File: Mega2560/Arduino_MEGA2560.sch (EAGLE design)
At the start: 8 parts

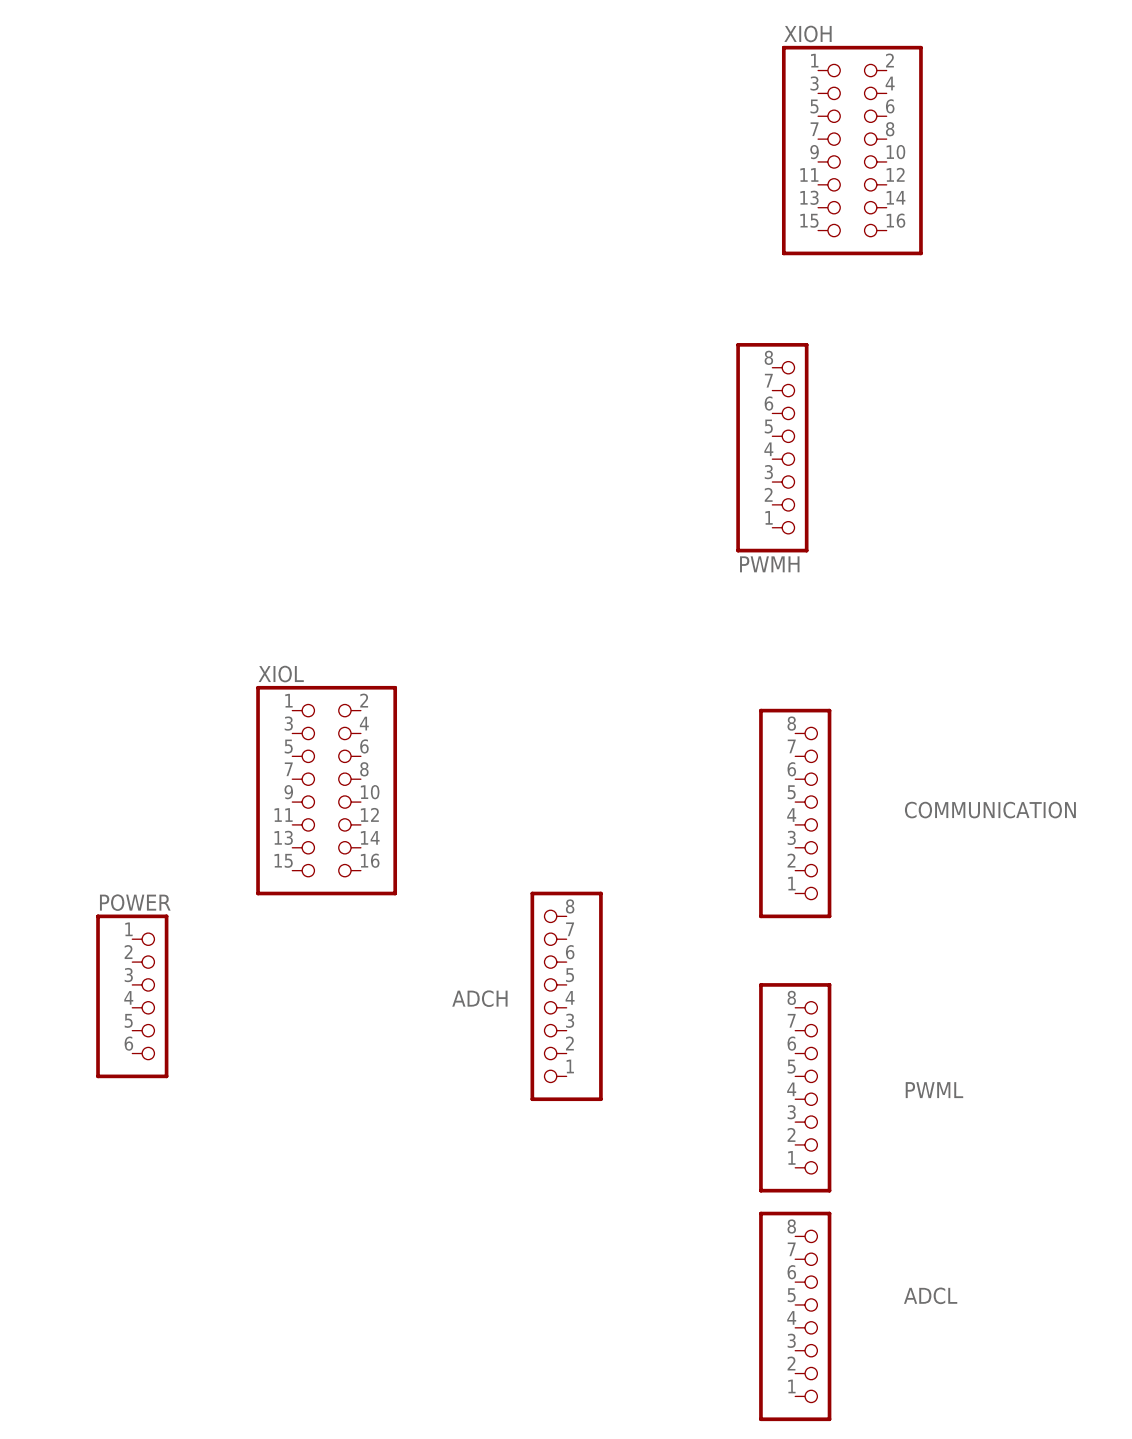
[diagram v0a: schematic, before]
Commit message: Arduino added ground pours
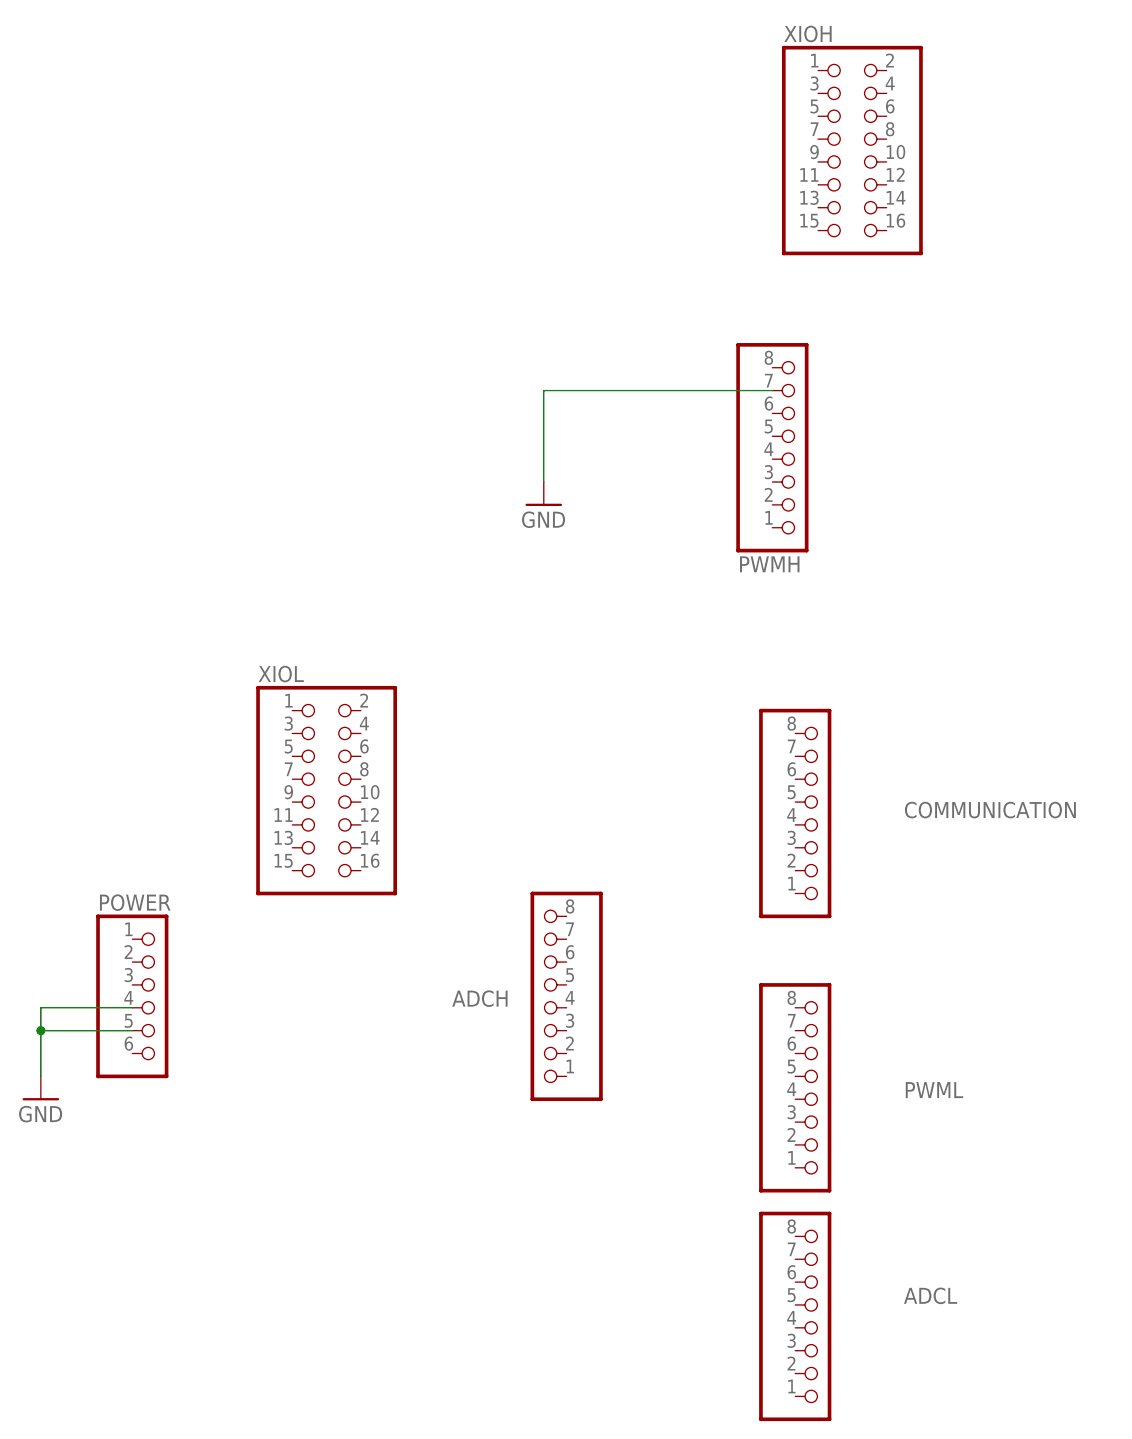
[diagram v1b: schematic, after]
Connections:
- new net GND: POWER.4, POWER.5, PWMH.7
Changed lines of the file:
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@@
 <part name="XIOH" library="pinhead" deviceset="PINHD-2X8" device=""/>
 <part name="XIOL" library="pinhead" deviceset="PINHD-2X8" device=""/>
+<part name="GND1" library="supply1" deviceset="GND" device=""/>
+<part name="GND2" library="supply1" deviceset="GND" device=""/>
 </parts>
 <sheets>
@@
 <instance part="XIOH" gate="A" x="101.6" y="137.16"/>
 <instance part="XIOL" gate="A" x="43.18" y="66.04"/>
+<instance part="GND1" gate="1" x="12.7" y="30.48"/>
+<instance part="GND2" gate="1" x="68.58" y="96.52"/>
 </instances>
 <busses>
 </busses>
 <nets>
+<net name="GND" class="0">
+<segment>
+<pinref part="POWER" gate="A" pin="4"/>
+<pinref part="GND1" gate="1" pin="GND"/>
+<wire x1="22.86" y1="40.64" x2="12.7" y2="40.64" width="0.1524" layer="91"/>
+<wire x1="12.7" y1="40.64" x2="12.7" y2="38.1" width="0.1524" layer="91"/>
+<pinref part="POWER" gate="A" pin="5"/>
+<wire x1="12.7" y1="38.1" x2="12.7" y2="33.02" width="0.1524" layer="91"/>
+<wire x1="22.86" y1="38.1" x2="12.7" y2="38.1" width="0.1524" layer="91"/>
+<junction x="12.7" y="38.1"/>
+</segment>
+<segment>
+<pinref part="PWMH" gate="A" pin="7"/>
+<pinref part="GND2" gate="1" pin="GND"/>
+<wire x1="93.98" y1="109.22" x2="68.58" y2="109.22" width="0.1524" layer="91"/>
+<wire x1="68.58" y1="109.22" x2="68.58" y2="99.06" width="0.1524" layer="91"/>
+</segment>
+</net>
 </nets>
 </sheet>
